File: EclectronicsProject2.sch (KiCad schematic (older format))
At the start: 1 part

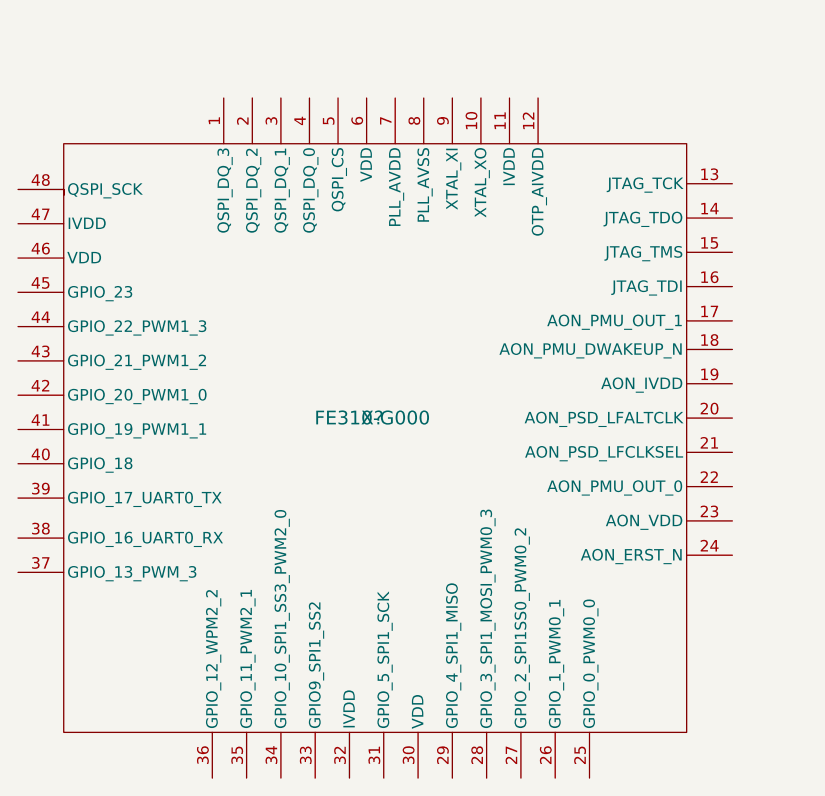
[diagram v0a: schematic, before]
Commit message: heatcamera schematic added
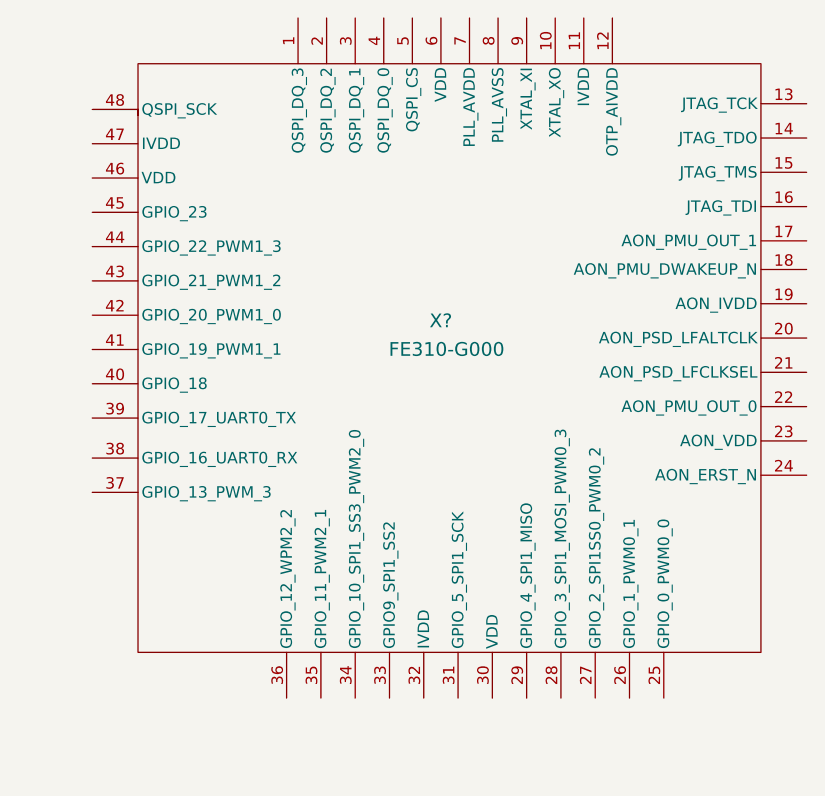
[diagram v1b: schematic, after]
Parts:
- removed X?: FE310-G000, symbol FE310-G000
- added X?: FE310-G000, symbol FE310-G000
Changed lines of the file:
@@
 EESchema Schematic File Version 2
+LIBS:EclectronicsProject2-rescue
 LIBS:power
 LIBS:device
@@
 LIBS:valves
 LIBS:newlib
+LIBS:EclectronicsProject2-cache
 EELAYER 25 0
 EELAYER END
@@
 $Comp
 L FE310-G000 X?
-U 1 1 59C97ACF
-P 4700 3675
-F 0 "X?" H 4700 3675 60  0000 C CNN
-F 1 "FE310-G000" H 4700 3675 60  0000 C CNN
-F 2 "" H 4700 3675 60  0001 C CNN
-F 3 "" H 4700 3675 60  0001 C CNN
-	1    4700 3675
+U 1 1 59C9C5C5
+P 5025 3325
+F 0 "X?" H 5000 3400 60  0000 C CNN
+F 1 "FE310-G000" H 5025 3275 60  0000 C CNN
+F 2 "" V 4750 3250 60  0001 C CNN
+F 3 "" V 4750 3250 60  0001 C CNN
+	1    5025 3325
 	1    0    0    -1
 $EndComp

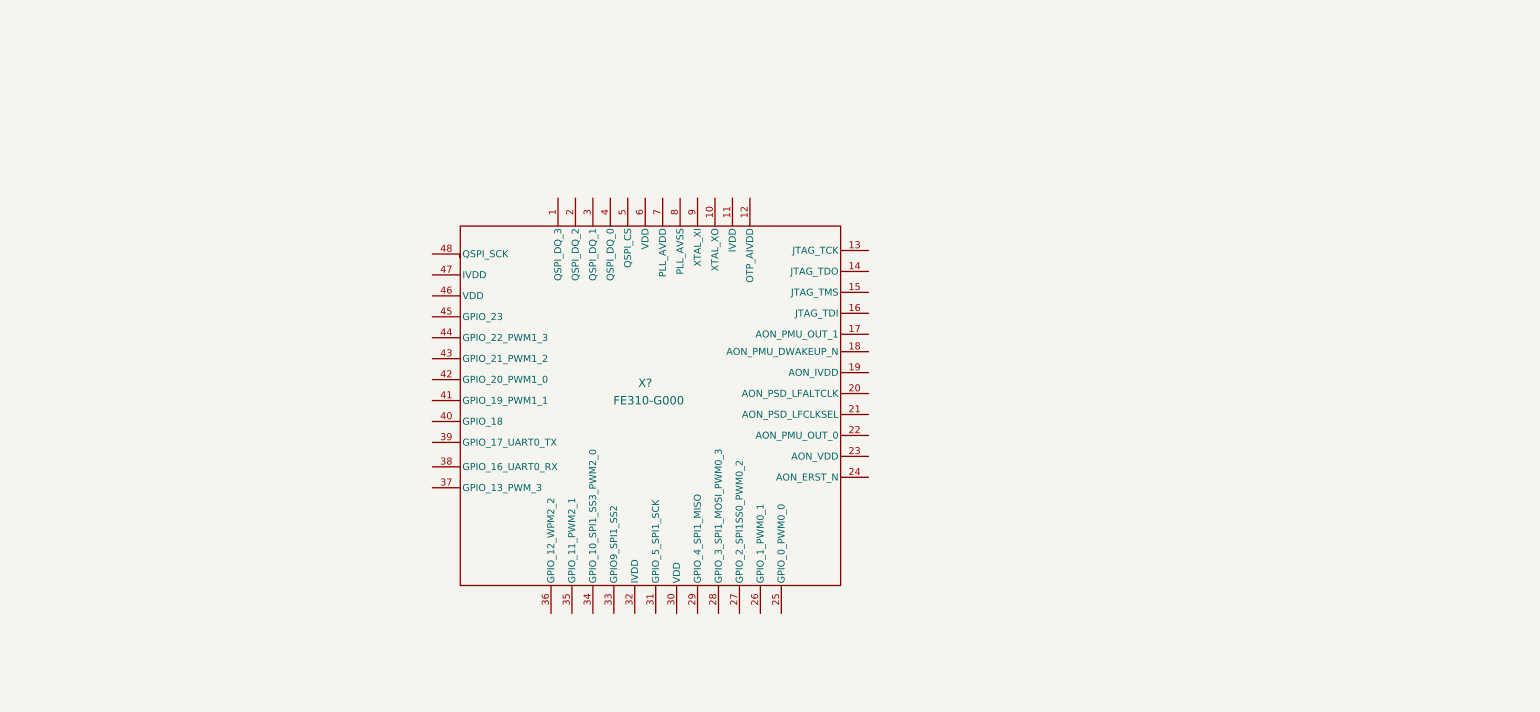
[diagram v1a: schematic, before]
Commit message: schmatic partial update
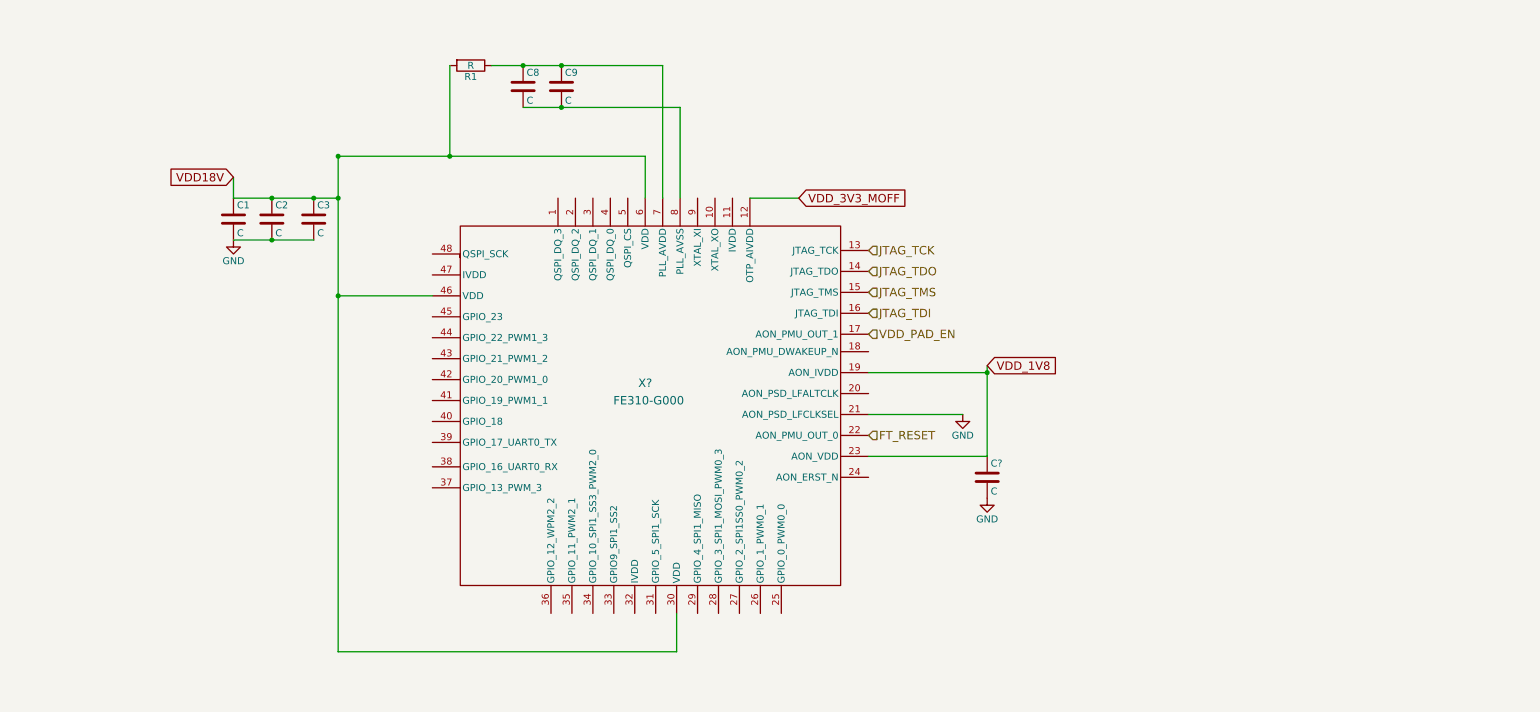
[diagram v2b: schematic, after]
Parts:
- added C1, C2, C3, C8, C9, C?: C, symbol C
- added R1: R, symbol R
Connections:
- net VDD_3V3_MOFF: now reaches X?.12 (OTP_AIVDD)
- net JTAG_TCK: now reaches X?.13 (JTAG_TCK)
- net JTAG_TDO: now reaches X?.14 (JTAG_TDO)
- net JTAG_TMS: now reaches X?.15 (JTAG_TMS)
- net JTAG_TDI: now reaches X?.16 (JTAG_TDI)
- net VDD_PAD_EN: now reaches X?.17 (AON_PMU_OUT_1)
- net VDD_1V8: now reaches X?.19 (AON_IVDD)
- net VDD_1V8: now also X?.23 (AON_VDD), C?.1
- net GND: now reaches X?.21 (AON_PSD_LFCLKSEL)
- net GND: now also C1.2, C2.2, C3.2, C?.2
- net FT_RESET: now reaches X?.22 (AON_PMU_OUT_0)
- net VDD18V: now reaches X?.30 (VDD)
- net VDD18V: now also X?.46 (VDD), X?.6 (VDD), C1.1, C2.1, C3.1, R1.2
- net at X?.7 (PLL_AVDD): now also C8.1, C9.1, R1.1
- net at X?.8 (PLL_AVSS): now also C8.2, C9.2
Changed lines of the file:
@@
 	1    0    0    -1
 $EndComp
+Wire Wire Line
+	5225 4900 5225 5175
+Wire Wire Line
+	5225 5175 2800 5175
+Wire Wire Line
+	2800 2625 3475 2625
+Connection ~ 2800 2625
+$Comp
+L C C3
+U 1 1 59CA9574
+P 2625 2075
+F 0 "C3" H 2650 2175 50  0000 L CNN
+F 1 "C" H 2650 1975 50  0000 L CNN
+F 2 "" H 2663 1925 50  0001 C CNN
+F 3 "" H 2625 2075 50  0001 C CNN
+	1    2625 2075
+	1    0    0    -1
+$EndComp
+$Comp
+L C C2
+U 1 1 59CA9611
+P 2325 2075
+F 0 "C2" H 2350 2175 50  0000 L CNN
+F 1 "C" H 2350 1975 50  0000 L CNN
+F 2 "" H 2363 1925 50  0001 C CNN
+F 3 "" H 2325 2075 50  0001 C CNN
+	1    2325 2075
+	1    0    0    -1
+$EndComp
+$Comp
+L C C1
+U 1 1 59CA963B
+P 2050 2075
+F 0 "C1" H 2075 2175 50  0000 L CNN
+F 1 "C" H 2075 1975 50  0000 L CNN
+F 2 "" H 2088 1925 50  0001 C CNN
+F 3 "" H 2050 2075 50  0001 C CNN
+	1    2050 2075
+	1    0    0    -1
+$EndComp
+Connection ~ 2800 1925
+Connection ~ 2625 1925
+Connection ~ 2325 1925
+Wire Wire Line
+	2050 2225 2625 2225
+Connection ~ 2325 2225
+Wire Wire Line
+	2050 1925 2800 1925
+$Comp
+L GND #PWR?
+U 1 1 59CA98BC
+P 2050 2225
+F 0 "#PWR?" H 2050 1975 50  0001 C CNN
+F 1 "GND" H 2050 2075 50  0000 C CNN
+F 2 "" H 2050 2225 50  0001 C CNN
+F 3 "" H 2050 2225 50  0001 C CNN
+	1    2050 2225
+	1    0    0    -1
+$EndComp
+Wire Wire Line
+	2050 1775 2050 1925
+Text GLabel 2050 1775 0    60   Input ~ 0
+VDD18V
+$Comp
+L C C8
+U 1 1 59CA9973
+P 4125 1125
+F 0 "C8" H 4150 1225 50  0000 L CNN
+F 1 "C" H 4150 1025 50  0000 L CNN
+F 2 "" H 4163 975 50  0001 C CNN
+F 3 "" H 4125 1125 50  0001 C CNN
+	1    4125 1125
+	1    0    0    -1
+$EndComp
+$Comp
+L C C9
+U 1 1 59CA99BA
+P 4400 1125
+F 0 "C9" H 4425 1225 50  0000 L CNN
+F 1 "C" H 4425 1025 50  0000 L CNN
+F 2 "" H 4438 975 50  0001 C CNN
+F 3 "" H 4400 1125 50  0001 C CNN
+	1    4400 1125
+	1    0    0    -1
+$EndComp
+Wire Wire Line
+	5125 975  5125 1925
+Wire Wire Line
+	3900 975  5125 975
+Connection ~ 4400 975
+Wire Wire Line
+	4125 1275 5250 1275
+Wire Wire Line
+	5250 1275 5250 1925
+Connection ~ 4400 1275
+Connection ~ 4125 975
+$Comp
+L R R1
+U 1 1 59CA9B32
+P 3750 975
+F 0 "R1" V 3830 975 50  0000 C CNN
+F 1 "R" V 3750 975 50  0000 C CNN
+F 2 "" V 3680 975 50  0001 C CNN
+F 3 "" H 3750 975 50  0001 C CNN
+	1    3750 975
+	0    1    1    0
+$EndComp
+Wire Wire Line
+	5000 1925 5000 1625
+Wire Wire Line
+	5000 1625 2800 1625
+Connection ~ 2800 1625
+Connection ~ 3600 1625
+Wire Wire Line
+	3600 975  3600 1625
+Wire Wire Line
+	2800 1625 2800 5175
+Wire Wire Line
+	5750 1925 6100 1925
+Text GLabel 6100 1925 2    60   Input ~ 0
+VDD_3V3_MOFF
+Wire Wire Line
+	7450 3775 6600 3775
+Wire Wire Line
+	7450 3125 7450 3775
+Wire Wire Line
+	7450 3175 6600 3175
+$Comp
+L C C?
+U 1 1 59CAAE5F
+P 7450 3925
+F 0 "C?" H 7475 4025 50  0000 L CNN
+F 1 "C" H 7475 3825 50  0000 L CNN
+F 2 "" H 7488 3775 50  0001 C CNN
+F 3 "" H 7450 3925 50  0001 C CNN
+	1    7450 3925
+	1    0    0    -1
+$EndComp
+$Comp
+L GND #PWR?
+U 1 1 59CAAED0
+P 7450 4075
+F 0 "#PWR?" H 7450 3825 50  0001 C CNN
+F 1 "GND" H 7450 3925 50  0000 C CNN
+F 2 "" H 7450 4075 50  0001 C CNN
+F 3 "" H 7450 4075 50  0001 C CNN
+	1    7450 4075
+	1    0    0    -1
+$EndComp
+Connection ~ 7450 3175
+Text GLabel 7450 3125 2    60   Input ~ 0
+VDD_1V8
+$Comp
+L GND #PWR?
+U 1 1 59CAB0F5
+P 7275 3475
+F 0 "#PWR?" H 7275 3225 50  0001 C CNN
+F 1 "GND" H 7275 3325 50  0000 C CNN
+F 2 "" H 7275 3475 50  0001 C CNN
+F 3 "" H 7275 3475 50  0001 C CNN
+	1    7275 3475
+	1    0    0    -1
+$EndComp
+Text HLabel 6600 2900 2    60   Input ~ 0
+VDD_PAD_EN
+Text HLabel 6600 3625 2    60   Input ~ 0
+FT_RESET
+Wire Wire Line
+	6600 3475 7275 3475
+Text HLabel 6600 2300 2    60   Input ~ 0
+JTAG_TCK
+Text HLabel 6600 2450 2    60   Input ~ 0
+JTAG_TDO
+Text HLabel 6600 2600 2    60   Input ~ 0
+JTAG_TMS
+Text HLabel 6600 2750 2    60   Input ~ 0
+JTAG_TDI
 $EndSCHEMATC

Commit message: added misc components to the library and updated the schematic
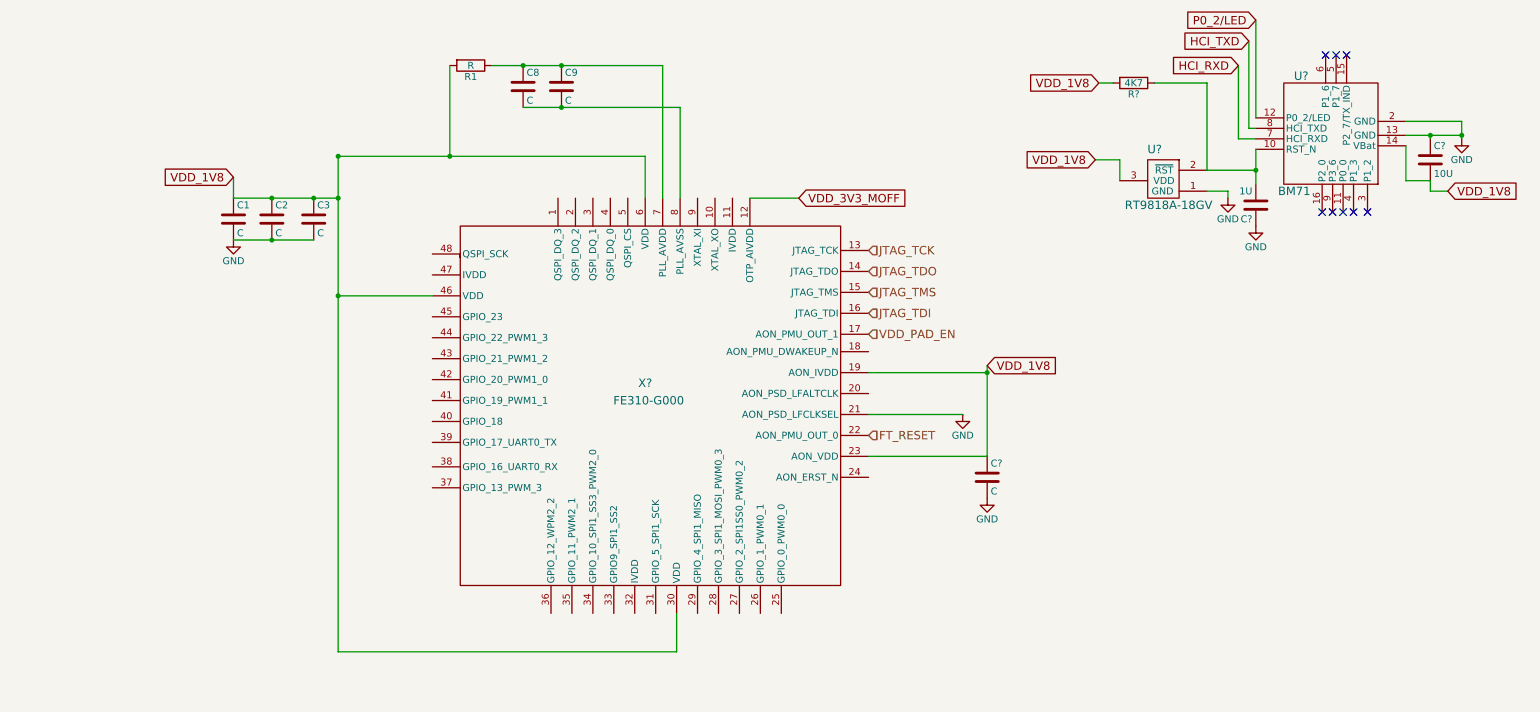
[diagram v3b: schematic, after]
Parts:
- added C?: 10U, symbol C
- added C?: 1U, symbol C
- added R?: 4K7, symbol R
- added U?: BM71, symbol BM71
- added U?: RT9818A-18GV, symbol RT9818A-18GV
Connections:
- net VDD18V is gone; now on net VDD_1V8: C1.1, C2.1, C3.1, R1.2, X?.30 (VDD), X?.46 (VDD), X?.6 (VDD)
- net GND: now also C?.1, C?.1, U?.1 (GND), U?.13 (GND), U?.2 (GND)
- net VDD_1V8: now also C?.2, R?.2, U?.14 (VBat), U?.3 (VDD)
- new net: C?.2, R?.1, U?.10 (RST_N), U?.2 (~RST)
- new net HCI_RXD: U?.7 (HCI_RXD)
- new net HCI_TXD: U?.8 (HCI_TXD)
- new net P0_2/LED: U?.12 (P0_2/LED)
- no-connect marks 0 -> 8
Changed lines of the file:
@@
 	2050 1775 2050 1925
 Text GLabel 2050 1775 0    60   Input ~ 0
-VDD18V
+VDD_1V8
 $Comp
 L C C8
@@
 Text HLabel 6600 2750 2    60   Input ~ 0
 JTAG_TDI
+$Comp
+L BM71 U?
+U 1 1 59CAB9AC
+P 9900 1450
+F 0 "U?" H 9700 1850 60  0000 C CNN
+F 1 "BM71" H 9650 1025 60  0000 C CNN
+F 2 "" H 10125 1175 60  0001 C CNN
+F 3 "" H 10125 1175 60  0001 C CNN
+	1    9900 1450
+	1    0    0    -1
+$EndComp
+$Comp
+L GND #PWR?
+U 1 1 59CABD8F
+P 10850 1500
+F 0 "#PWR?" H 10850 1250 50  0001 C CNN
+F 1 "GND" H 10850 1350 50  0000 C CNN
+F 2 "" H 10850 1500 50  0001 C CNN
+F 3 "" H 10850 1500 50  0001 C CNN
+	1    10850 1500
+	1    0    0    -1
+$EndComp
+Wire Wire Line
+	10450 1375 10850 1375
+Wire Wire Line
+	10850 1375 10850 1500
+Wire Wire Line
+	10450 1475 10850 1475
+Connection ~ 10850 1475
+Text GLabel 10750 1875 2    60   Input ~ 0
+VDD_1V8
+Wire Wire Line
+	10450 1550 10450 1800
+$Comp
+L C C?
+U 1 1 59CABEAE
+P 10625 1650
+F 0 "C?" H 10650 1750 50  0000 L CNN
+F 1 "10U" H 10650 1550 50  0000 L CNN
+F 2 "" H 10663 1500 50  0001 C CNN
+F 3 "" H 10625 1650 50  0001 C CNN
+	1    10625 1650
+	1    0    0    -1
+$EndComp
+Wire Wire Line
+	10625 1500 10625 1475
+Connection ~ 10625 1475
+Wire Wire Line
+	10450 1800 10625 1800
+Wire Wire Line
+	10750 1875 10625 1875
+Wire Wire Line
+	10625 1875 10625 1800
+$Comp
+L RT9818A-18GV U?
+U 1 1 59CAC0D5
+P 8725 1800
+F 0 "U?" H 8650 2025 60  0000 C CNN
+F 1 "RT9818A-18GV" H 8750 1625 60  0000 C CNN
+F 2 "" H 8725 1800 60  0001 C CNN
+F 3 "" H 8725 1800 60  0001 C CNN
+	1    8725 1800
+	1    0    0    -1
+$EndComp
+Text GLabel 8225 1650 0    60   Input ~ 0
+VDD_1V8
+Wire Wire Line
+	8225 1650 8400 1650
+Wire Wire Line
+	8400 1650 8400 1800
+$Comp
+L GND #PWR?
+U 1 1 59CAC1A4
+P 9175 1925
+F 0 "#PWR?" H 9175 1675 50  0001 C CNN
+F 1 "GND" H 9175 1775 50  0000 C CNN
+F 2 "" H 9175 1925 50  0001 C CNN
+F 3 "" H 9175 1925 50  0001 C CNN
+	1    9175 1925
+	1    0    0    -1
+$EndComp
+Wire Wire Line
+	9175 1925 9175 1875
+Wire Wire Line
+	9175 1875 9025 1875
+Text GLabel 8250 1100 0    60   Input ~ 0
+VDD_1V8
+$Comp
+L GND #PWR?
+U 1 1 59CAC236
+P 9375 2125
+F 0 "#PWR?" H 9375 1875 50  0001 C CNN
+F 1 "GND" H 9375 1975 50  0000 C CNN
+F 2 "" H 9375 2125 50  0001 C CNN
+F 3 "" H 9375 2125 50  0001 C CNN
+	1    9375 2125
+	1    0    0    -1
+$EndComp
+$Comp
+L R R?
+U 1 1 59CAC324
+P 8500 1100
+F 0 "R?" V 8580 1100 50  0000 C CNN
+F 1 "4K7" V 8500 1100 50  0000 C CNN
+F 2 "" V 8430 1100 50  0001 C CNN
+F 3 "" H 8500 1100 50  0001 C CNN
+	1    8500 1100
+	0    1    1    0
+$EndComp
+Wire Wire Line
+	8250 1100 8350 1100
+$Comp
+L C C?
+U 1 1 59CAC446
+P 9375 1975
+F 0 "C?" H 9400 2075 50  0000 L CNN
+F 1 "1U" H 9400 1875 50  0000 L CNN
+F 2 "" H 9413 1825 50  0001 C CNN
+F 3 "" H 9375 1975 50  0001 C CNN
+	1    9375 1975
+	-1   0    0    1
+$EndComp
+Wire Wire Line
+	8650 1100 9025 1100
+Wire Wire Line
+	9025 1100 9025 1725
+Wire Wire Line
+	9025 1725 9375 1725
+Wire Wire Line
+	9375 1575 9375 1825
+Connection ~ 9375 1725
+Wire Wire Line
+	9375 650  9375 1350
+Wire Wire Line
+	9375 1425 9325 1425
+Wire Wire Line
+	9325 1425 9325 800
+Wire Wire Line
+	9375 1500 9250 1500
+Text GLabel 9325 800  0    60   Input ~ 0
+HCI_TXD
+Wire Wire Line
+	9250 1500 9250 975
+Text GLabel 9250 975  0    60   Input ~ 0
+HCI_RXD
+Text GLabel 9375 650  0    60   Input ~ 0
+P0_2/LED
+NoConn ~ 9850 2025
+NoConn ~ 9925 2025
+NoConn ~ 10000 2025
+NoConn ~ 10075 2025
+NoConn ~ 10175 2025
+NoConn ~ 9875 900
+NoConn ~ 9950 900
+NoConn ~ 10025 900
 $EndSCHEMATC

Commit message: updated schematic and added parts to library
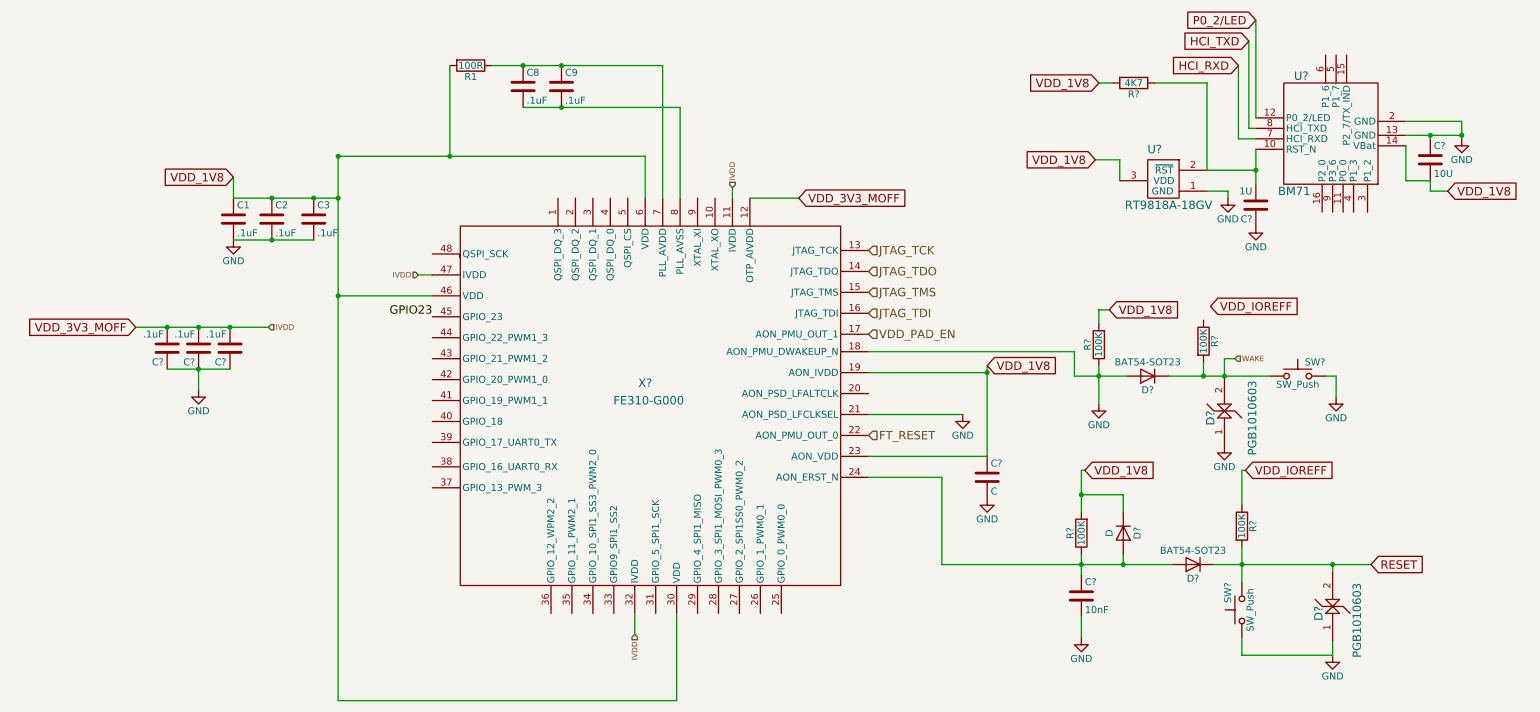
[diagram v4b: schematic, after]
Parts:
- added C?: 10nF, symbol C
- added C? (x3): .1uF, symbol C
- added D?: D, symbol D
- added D? (x2): BAT54-SOT23, symbol D
- added D? (x2): PGB1010603, symbol PGB1010603
- added R? (x4): 100K, symbol R
- added SW? (x2): SW_Push, symbol SW_Push
- C1, C2, C3, C8, C9: value C -> .1uF
- R1: value R -> 100R
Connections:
- net GND: now also X?.18 (AON_PMU_DWAKEUP_N), C?.1, C?.1, C?.1, C?.2, D?.1, D?.1, D?.2 (A), R?.1, SW?.1, SW?.2
- net VDD_1V8: now also D?.1 (K), R?.2, R?.2
- net VDD_3V3_MOFF: now also X?.11 (IVDD), X?.32 (IVDD), X?.47 (IVDD), C?.2, C?.2, C?.2
- net at X?.24 (AON_ERST_N): now also C?.1, D?.2 (A), D?.2 (A), R?.1
- net GPIO23: now reaches X?.45 (GPIO_23)
- new net RESET: D?.1 (K), D?.2, R?.2, SW?.2
- new net VDD_IOREFF: R?.1
- new net WAKE: D?.1 (K), D?.2, R?.2, SW?.1
- no-connect marks 8 -> 0
